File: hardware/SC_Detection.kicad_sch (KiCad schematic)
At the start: 38 parts, among them U13 LMV393IDGKR, U14 LMV393IDGKR, U15 LMV393IDGKR, U16 LMV393IDGKR, U17 INA181, U18 INA181, U19 INA181, U20 INA181, U21 REF2033

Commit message: update bom
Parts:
- R39, R42, R43, R46, R47, R50, R51, R54: Manufacturer (none) -> YAGEO; Manufacturer Number (none) -> RC0402FR-0731K6L
- R40, R41, R44, R45, R48, R49, R52, R53: Link (none) -> https://www.digikey.com/en/products/detail/panasonic-electr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; Manufacturer (none) -> Panasonic Electronic Components; Manufacturer Number (none) -> ERJ-2RKF1001X
- R55, R56, R57, R58: Link (none) -> https://www.digikey.com/en/products/detail/samsung-electro-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; Manufacturer (none) -> Samsung Electro-Mechanics; Manufacturer Number (none) -> RC1005F103CS
- U17, U18, U19, U20: value INA181 -> INA181A1; Link (none) -> https://www.digikey.com/en/products/detail/texas-instrument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; Manufacturer Number INA181A4 -> INA181A1QDBVRQ1

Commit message: update missing footprints to meet min pad mask clearance
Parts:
- U13, U14, U15, U16: footprint Package_SO:VSSOP-8_3x3mm_P0.65mm -> kicad-lib:VSSOP-8_3x3mm_P0.65mm_TexasInstruments
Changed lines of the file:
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@@
 			)
 		)
-		(property "Footprint" "Package_SO:VSSOP-8_3x3mm_P0.65mm"
+		(property "Footprint" "kicad-lib:VSSOP-8_3x3mm_P0.65mm_TexasInstruments"
 			(at 30.48 46.99 0)
 			(effects
@@
 			)
 		)
-		(property "Footprint" "Package_SO:VSSOP-8_3x3mm_P0.65mm"
+		(property "Footprint" "kicad-lib:VSSOP-8_3x3mm_P0.65mm_TexasInstruments"
 			(at 30.48 172.72 0)
 			(effects
@@
 			)
 		)
-		(property "Footprint" "Package_SO:VSSOP-8_3x3mm_P0.65mm"
+		(property "Footprint" "kicad-lib:VSSOP-8_3x3mm_P0.65mm_TexasInstruments"
 			(at 139.7 179.07 0)
 			(effects
@@
 			)
 		)
-		(property "Footprint" "Package_SO:VSSOP-8_3x3mm_P0.65mm"
+		(property "Footprint" "kicad-lib:VSSOP-8_3x3mm_P0.65mm_TexasInstruments"
 			(at 139.7 82.55 0)
 			(effects
@@
 			)
 		)
-		(property "Footprint" "Package_SO:VSSOP-8_3x3mm_P0.65mm"
+		(property "Footprint" "kicad-lib:VSSOP-8_3x3mm_P0.65mm_TexasInstruments"
 			(at 139.7 124.46 0)
 			(effects
@@
 			)
 		)
-		(property "Footprint" "Package_SO:VSSOP-8_3x3mm_P0.65mm"
+		(property "Footprint" "kicad-lib:VSSOP-8_3x3mm_P0.65mm_TexasInstruments"
 			(at 139.7 40.64 0)
 			(effects
@@
 			)
 		)
-		(property "Footprint" "Package_SO:VSSOP-8_3x3mm_P0.65mm"
+		(property "Footprint" "kicad-lib:VSSOP-8_3x3mm_P0.65mm_TexasInstruments"
 			(at 139.7 166.37 0)
 			(effects
@@
 			)
 		)
-		(property "Footprint" "Package_SO:VSSOP-8_3x3mm_P0.65mm"
+		(property "Footprint" "kicad-lib:VSSOP-8_3x3mm_P0.65mm_TexasInstruments"
 			(at 30.48 88.9 0)
 			(effects
@@
 			)
 		)
-		(property "Footprint" "Package_SO:VSSOP-8_3x3mm_P0.65mm"
+		(property "Footprint" "kicad-lib:VSSOP-8_3x3mm_P0.65mm_TexasInstruments"
 			(at 139.7 137.16 0)
 			(effects
@@
 			)
 		)
-		(property "Footprint" "Package_SO:VSSOP-8_3x3mm_P0.65mm"
+		(property "Footprint" "kicad-lib:VSSOP-8_3x3mm_P0.65mm_TexasInstruments"
 			(at 30.48 130.81 0)
 			(effects
@@
 			)
 		)
-		(property "Footprint" "Package_SO:VSSOP-8_3x3mm_P0.65mm"
+		(property "Footprint" "kicad-lib:VSSOP-8_3x3mm_P0.65mm_TexasInstruments"
 			(at 139.7 53.34 0)
 			(effects
@@
 			)
 		)
-		(property "Footprint" "Package_SO:VSSOP-8_3x3mm_P0.65mm"
+		(property "Footprint" "kicad-lib:VSSOP-8_3x3mm_P0.65mm_TexasInstruments"
 			(at 139.7 95.25 0)
 			(effects

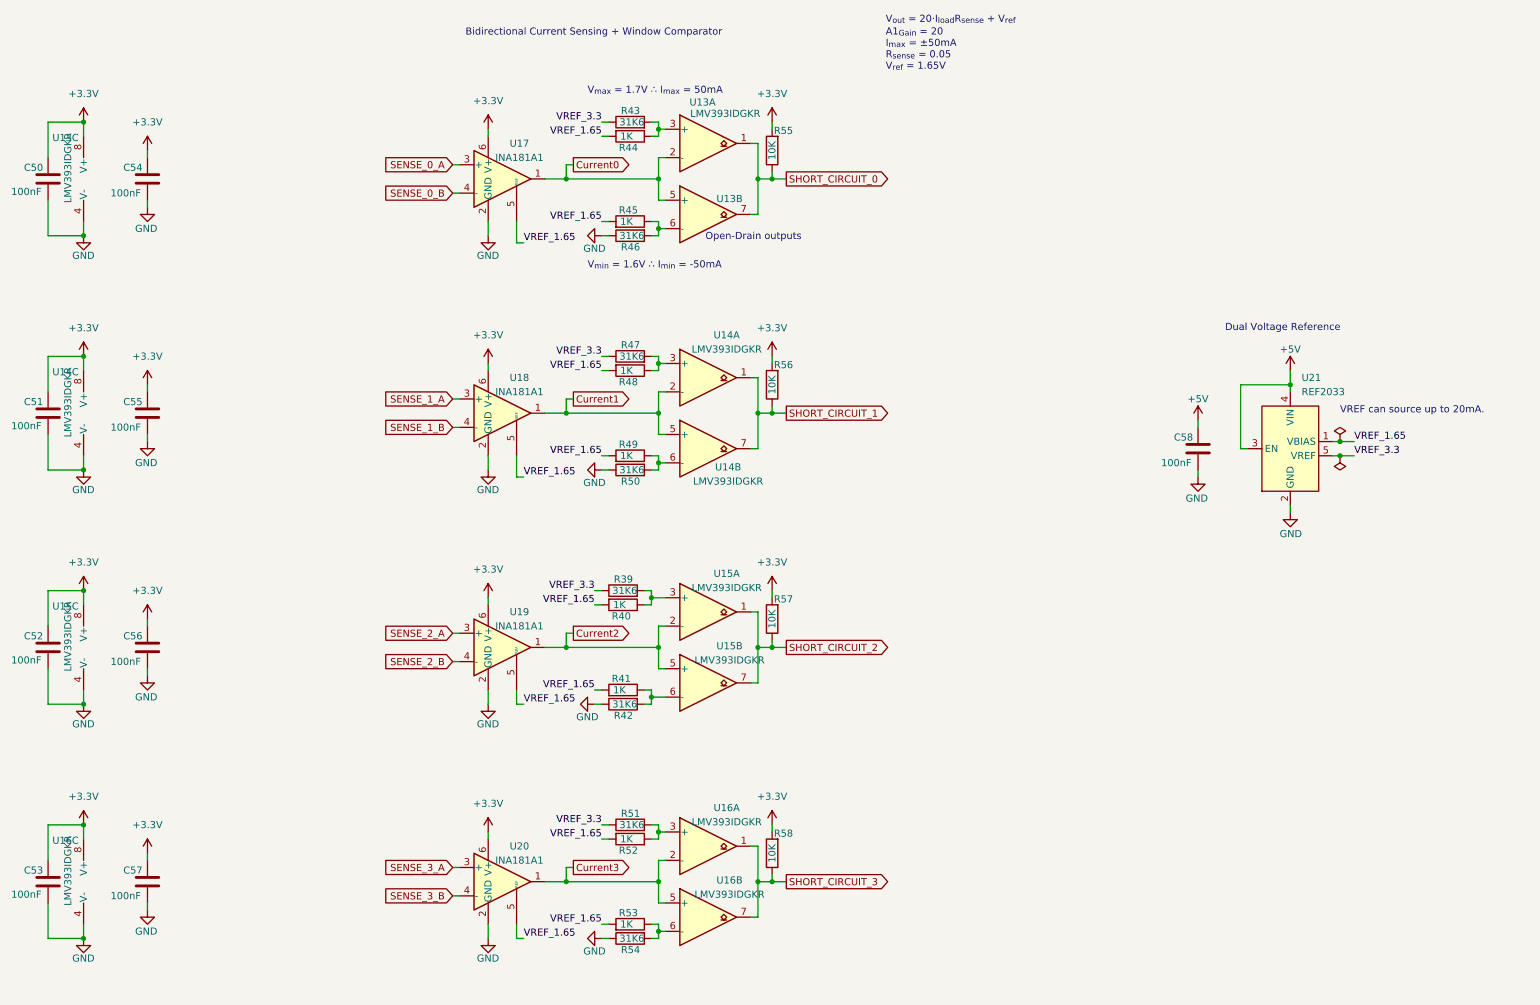
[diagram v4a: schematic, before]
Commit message: feat pcba updates (#69)
* replace INA181 w INA630

* flip c12; put ext triggers on gpio multiple of 8

* add pulldowns to external triggers

* change R3, R15, R16, R20, R21 package to 0402

* update 1K, 31K6, 10K resistors to 0.1%

* swap BNC connectors to taller versions

* move short-circuit pins to fall within multiple of 8 boundary

* add 1.0/1.1 hw pinout to config with default as 1.0

* update hardware author
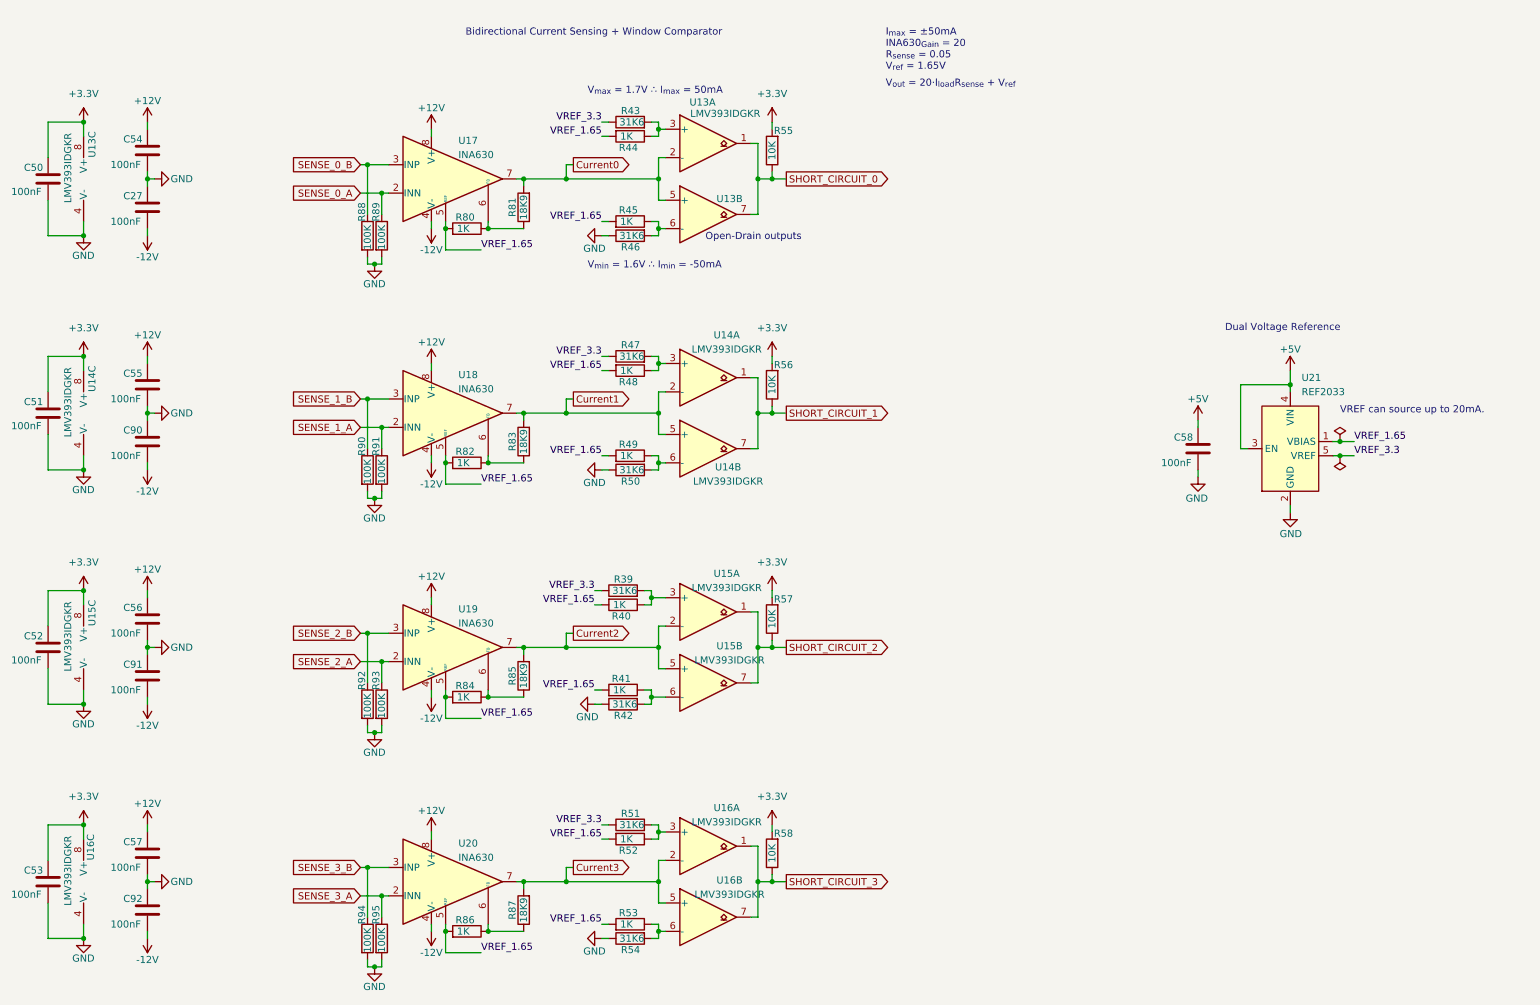
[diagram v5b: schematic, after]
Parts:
- removed U17, U18, U19, U20: INA181A1, Package_TO_SOT_SMD:SOT-23-6, symbol Amplifier_Current:INA181
- added C27, C90, C91, C92: 100nF, Capacitor_SMD:C_0402_1005Metric, symbol Device:C
- added R80, R82, R84, R86: 1K, Resistor_SMD:R_0402_1005Metric, symbol Device:R
- added R81, R83, R85, R87: 18K9, Resistor_SMD:R_0402_1005Metric, symbol Device:R
- added R88, R89, R90, R91, R92, R93, R94, R95: 100K, Resistor_SMD:R_0402_1005Metric, symbol Device:R
- added U17, U18, U19, U20: INA630, kicad-lib:TSOT-23-8, symbol kicad-lib:INA630
- R39, R42, R43, R46, R47, R50, R51, R54: Link (none) -> https://www.digikey.com/en/products/detail/yageo/RT0402BRD0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; Manufacturer Number RC0402FR-0731K6L -> RT0402BRD0731K6L
- R40, R41, R44, R45, R48, R49, R52, R53: Link https://www.digikey.com/en/products/detail/panasonic-electr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 -> https://www.digikey.com/en/products/detail/yageo/RT0402BRE0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; Manufacturer Panasonic Electronic Components -> YAGEO; Manufacturer Number ERJ-2RKF1001X -> RT0402BRE071KL; Tolerance (none) -> 0.1%
- R55, R56, R57, R58: Link https://www.digikey.com/en/products/detail/samsung-electro-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 -> https://www.digikey.com/en/products/detail/yageo/RT0402BRD0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; Manufacturer Samsung Electro-Mechanics -> YAGEO; Manufacturer Number RC1005F103CS -> RT0402BRD0710KL; Tolerance (none) -> 0.1%
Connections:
- net +3.3V: no longer C54.1, C55.1, C56.1, C57.1
- net Current0: now also R81.2, U17.7
- net Current1: now also R83.2, U18.7
- net Current2: now also R85.2, U19.7
- net Current3: now also R87.2, U20.7
- net GND: now also C27.1, C90.1, C91.1, C92.1, R88.2, R89.2, R90.2, R91.2, R92.2, R93.2, R94.2, R95.2
- net SENSE_0_A: now also R89.1, U17.2 (INN)
- net SENSE_0_B: now also R88.1, U17.3 (INP)
- net SENSE_1_A: now also R91.1, U18.2 (INN)
- net SENSE_1_B: now also R90.1, U18.3 (INP)
- net SENSE_2_A: now also R93.1, U19.2 (INN)
- net SENSE_2_B: now also R92.1, U19.3 (INP)
- net SENSE_3_A: now also R95.1, U20.2 (INN)
- net SENSE_3_B: now also R94.1, U20.3 (INP)
- net VREF_1.65: now also R80.2, R82.2, R84.2, R86.2, U17.5 (REF), U18.5 (REF), U19.5 (REF), U20.5 (REF)
- new net: R86.1, R87.1, U20.6 (FB)
- new net: R84.1, R85.1, U19.6 (FB)
- new net: R82.1, R83.1, U18.6 (FB)
- new net: R80.1, R81.1, U17.6 (FB)
- new net +12V: C54.1, C55.1, C56.1, C57.1, U17.8 (V+), U18.8 (V+), U19.8 (V+), U20.8 (V+)
- new net -12V: C27.2, C90.2, C91.2, C92.2, U17.4 (V-), U18.4 (V-), U19.4 (V-), U20.4 (V-)
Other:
- note added: "I_{max} = ±50mA INA630_{Gain} = 20 R_{sense} = 0.05 V_{ref} = 1.65V"
- note removed: "A1_{Gain} = 20 I_{max} = ±50mA R_{sense} = 0.05 V_{ref} = 1.65V"
- moved on the sheet: C54, C55, C56, C57
